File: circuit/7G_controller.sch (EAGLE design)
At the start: 19 parts, among them Q1 3.6864MHz

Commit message: 
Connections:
- new net AREF: ATMEGA169PV.AREF
- net N$5: no longer C5.+
- net N$6: now also C5.+
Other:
- moved on the sheet: C5
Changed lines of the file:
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@@
 <part name="P+5" library="SparkFun" deviceset="VCC" device=""/>
 <part name="GND4" library="SparkFun" deviceset="GND" device=""/>
+<part name="GND8" library="SparkFun" deviceset="GND" device=""/>
 </parts>
 <sheets>
@@
 <instance part="P+10" gate="1" x="63.5" y="-20.32"/>
 <instance part="GND7" gate="1" x="63.5" y="-35.56"/>
-<instance part="C5" gate="G$1" x="157.48" y="35.56"/>
+<instance part="C5" gate="G$1" x="142.24" y="58.42" rot="R270"/>
 <instance part="R2" gate="G$1" x="132.08" y="-7.62"/>
 <instance part="R3" gate="G$1" x="114.3" y="-2.54"/>
@@
 <instance part="P+5" gate="1" x="-43.18" y="12.7"/>
 <instance part="GND4" gate="1" x="-45.72" y="25.4" rot="R90"/>
+<instance part="GND8" gate="1" x="129.54" y="50.8"/>
 </instances>
 <busses>
@@
 </segment>
 <segment>
+<pinref part="GND6" gate="1" pin="GND"/>
 <pinref part="LP2980" gate="G$1" pin="GND"/>
-<pinref part="GND6" gate="1" pin="GND"/>
-<wire x1="170.18" y1="30.48" x2="170.18" y2="27.94" width="0.1524" layer="91"/>
-<pinref part="C5" gate="G$1" pin="-"/>
-<wire x1="170.18" y1="27.94" x2="170.18" y2="25.4" width="0.1524" layer="91"/>
-<wire x1="157.48" y1="30.48" x2="157.48" y2="27.94" width="0.1524" layer="91"/>
-<wire x1="157.48" y1="27.94" x2="170.18" y2="27.94" width="0.1524" layer="91"/>
-<junction x="170.18" y="27.94"/>
+<wire x1="170.18" y1="30.48" x2="170.18" y2="25.4" width="0.1524" layer="91"/>
 </segment>
 <segment>
@@
 <wire x1="-58.42" y1="15.24" x2="-58.42" y2="17.78" width="0.1524" layer="91"/>
 <junction x="-58.42" y="17.78"/>
+</segment>
+<segment>
+<pinref part="C5" gate="G$1" pin="-"/>
+<wire x1="137.16" y1="58.42" x2="129.54" y2="58.42" width="0.1524" layer="91"/>
+<wire x1="129.54" y1="58.42" x2="129.54" y2="53.34" width="0.1524" layer="91"/>
+<pinref part="GND8" gate="1" pin="GND"/>
 </segment>
 </net>
@@
 <pinref part="SJ1" gate="G$1" pin="2"/>
 <wire x1="149.86" y1="58.42" x2="149.86" y2="48.26" width="0.1524" layer="91"/>
+<pinref part="C5" gate="G$1" pin="+"/>
+<wire x1="144.78" y1="58.42" x2="149.86" y2="58.42" width="0.1524" layer="91"/>
+<junction x="149.86" y="58.42"/>
 </segment>
 </net>
@@
 <pinref part="SJ1" gate="G$1" pin="1"/>
 <pinref part="LP2980" gate="G$1" pin="VOUT"/>
-<wire x1="154.94" y1="43.18" x2="157.48" y2="43.18" width="0.1524" layer="91"/>
-<pinref part="C5" gate="G$1" pin="+"/>
-<wire x1="157.48" y1="43.18" x2="160.02" y2="43.18" width="0.1524" layer="91"/>
-<wire x1="157.48" y1="43.18" x2="157.48" y2="38.1" width="0.1524" layer="91"/>
-<junction x="157.48" y="43.18"/>
+<wire x1="154.94" y1="43.18" x2="160.02" y2="43.18" width="0.1524" layer="91"/>
 </segment>
 </net>
@@
 </segment>
 </net>
+<net name="AREF" class="0">
+<segment>
+<pinref part="ATMEGA169PV" gate="G$1" pin="AREF"/>
+<wire x1="-7.62" y1="83.82" x2="-15.24" y2="83.82" width="0.1524" layer="91"/>
+</segment>
+</net>

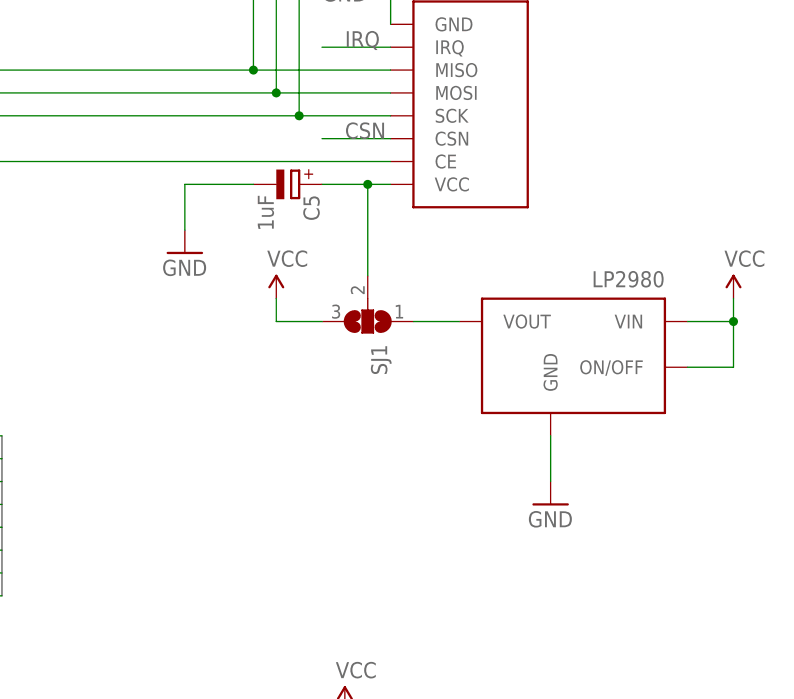
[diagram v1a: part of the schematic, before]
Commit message: 
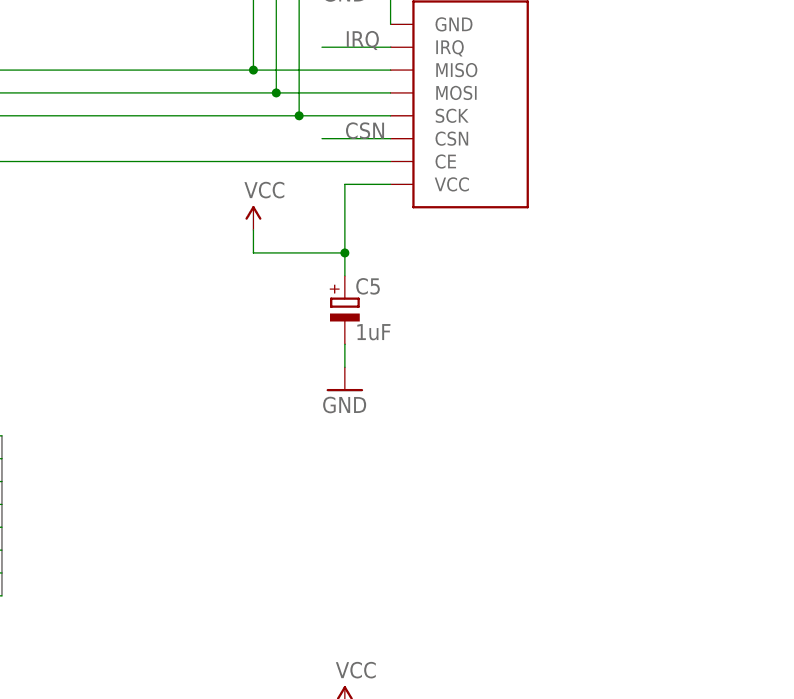
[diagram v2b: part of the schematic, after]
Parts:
- removed LP2980: LP2980, KileParts:LP2980
- removed SJ1: (no value), jumper:SJ2W
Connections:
- removed net N$5: LP2980.VOUT, SJ1.1
- removed net N$6: C5.+, NRF24L01.VCC, SJ1.2
- net GND: no longer LP2980.GND
- net VCC: now also C5.+, NRF24L01.VCC; no longer LP2980.ON/OFF, LP2980.VIN, SJ1.3
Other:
- moved on the sheet: C5
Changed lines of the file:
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@@
 <part name="P+7" library="SparkFun" deviceset="VCC" device=""/>
 <part name="P+8" library="SparkFun" deviceset="VCC" device=""/>
-<part name="LP2980" library="KileParts" deviceset="LP2980" device=""/>
-<part name="P+2" library="SparkFun" deviceset="VCC" device=""/>
-<part name="GND6" library="SparkFun" deviceset="GND" device=""/>
-<part name="SJ1" library="jumper" deviceset="SJ2W" device=""/>
-<part name="P+9" library="SparkFun" deviceset="VCC" device=""/>
 <part name="UART" library="KileParts" deviceset="UART_PORT" device=""/>
 <part name="P+10" library="SparkFun" deviceset="VCC" device=""/>
@@
 <part name="GND4" library="SparkFun" deviceset="GND" device=""/>
 <part name="GND8" library="SparkFun" deviceset="GND" device=""/>
+<part name="P+2" library="SparkFun" deviceset="VCC" device=""/>
 </parts>
 <sheets>
@@
 <instance part="P+7" gate="1" x="147.32" y="0"/>
 <instance part="P+8" gate="1" x="-15.24" y="-7.62"/>
-<instance part="LP2980" gate="G$1" x="172.72" y="38.1" rot="MR0"/>
-<instance part="P+2" gate="1" x="139.7" y="45.72"/>
-<instance part="GND6" gate="1" x="170.18" y="22.86"/>
-<instance part="SJ1" gate="G$1" x="149.86" y="43.18" rot="R270"/>
-<instance part="P+9" gate="1" x="190.5" y="45.72"/>
 <instance part="UART" gate="1" x="43.18" y="-25.4" rot="MR180"/>
 <instance part="P+10" gate="1" x="63.5" y="-20.32"/>
 <instance part="GND7" gate="1" x="63.5" y="-35.56"/>
-<instance part="C5" gate="G$1" x="142.24" y="58.42" rot="R270"/>
+<instance part="C5" gate="G$1" x="147.32" y="45.72"/>
 <instance part="R2" gate="G$1" x="132.08" y="-7.62"/>
 <instance part="R3" gate="G$1" x="114.3" y="-2.54"/>
@@
 <instance part="P+5" gate="1" x="-43.18" y="12.7"/>
 <instance part="GND4" gate="1" x="-45.72" y="25.4" rot="R90"/>
-<instance part="GND8" gate="1" x="129.54" y="50.8"/>
+<instance part="GND8" gate="1" x="147.32" y="35.56"/>
+<instance part="P+2" gate="1" x="137.16" y="53.34"/>
 </instances>
 <busses>
@@
 </segment>
 <segment>
-<pinref part="SJ1" gate="G$1" pin="3"/>
-<pinref part="P+2" gate="1" pin="VCC"/>
-<wire x1="144.78" y1="43.18" x2="139.7" y2="43.18" width="0.1524" layer="91"/>
-<wire x1="139.7" y1="43.18" x2="139.7" y2="45.72" width="0.1524" layer="91"/>
-</segment>
-<segment>
-<pinref part="LP2980" gate="G$1" pin="VIN"/>
-<pinref part="P+9" gate="1" pin="VCC"/>
-<wire x1="185.42" y1="43.18" x2="190.5" y2="43.18" width="0.1524" layer="91"/>
-<wire x1="190.5" y1="43.18" x2="190.5" y2="45.72" width="0.1524" layer="91"/>
-<pinref part="LP2980" gate="G$1" pin="ON/OFF"/>
-<wire x1="185.42" y1="38.1" x2="190.5" y2="38.1" width="0.1524" layer="91"/>
-<wire x1="190.5" y1="38.1" x2="190.5" y2="43.18" width="0.1524" layer="91"/>
-<junction x="190.5" y="43.18"/>
-</segment>
-<segment>
 <pinref part="UART" gate="1" pin="TX"/>
 <wire x1="50.8" y1="-25.4" x2="63.5" y2="-25.4" width="0.1524" layer="91"/>
@@
 <wire x1="-60.96" y1="10.16" x2="-43.18" y2="10.16" width="0.1524" layer="91"/>
 <wire x1="-43.18" y1="10.16" x2="-43.18" y2="12.7" width="0.1524" layer="91"/>
+</segment>
+<segment>
+<pinref part="NRF24L01" gate="G$1" pin="VCC"/>
+<pinref part="C5" gate="G$1" pin="+"/>
+<wire x1="147.32" y1="48.26" x2="147.32" y2="50.8" width="0.1524" layer="91"/>
+<wire x1="147.32" y1="50.8" x2="147.32" y2="58.42" width="0.1524" layer="91"/>
+<wire x1="147.32" y1="58.42" x2="152.4" y2="58.42" width="0.1524" layer="91"/>
+<pinref part="P+2" gate="1" pin="VCC"/>
+<wire x1="137.16" y1="53.34" x2="137.16" y2="50.8" width="0.1524" layer="91"/>
+<wire x1="137.16" y1="50.8" x2="147.32" y2="50.8" width="0.1524" layer="91"/>
+<junction x="147.32" y="50.8"/>
 </segment>
 </net>
@@
 </segment>
 <segment>
-<pinref part="GND6" gate="1" pin="GND"/>
-<pinref part="LP2980" gate="G$1" pin="GND"/>
-<wire x1="170.18" y1="30.48" x2="170.18" y2="25.4" width="0.1524" layer="91"/>
-</segment>
-<segment>
 <pinref part="UART" gate="1" pin="RX"/>
 <wire x1="50.8" y1="-27.94" x2="63.5" y2="-27.94" width="0.1524" layer="91"/>
@@
 <segment>
 <pinref part="C5" gate="G$1" pin="-"/>
-<wire x1="137.16" y1="58.42" x2="129.54" y2="58.42" width="0.1524" layer="91"/>
-<wire x1="129.54" y1="58.42" x2="129.54" y2="53.34" width="0.1524" layer="91"/>
 <pinref part="GND8" gate="1" pin="GND"/>
+<wire x1="147.32" y1="38.1" x2="147.32" y2="40.64" width="0.1524" layer="91"/>
 </segment>
 </net>
@@
 </segment>
 </net>
-<net name="N$6" class="0">
-<segment>
-<pinref part="NRF24L01" gate="G$1" pin="VCC"/>
-<wire x1="149.86" y1="58.42" x2="152.4" y2="58.42" width="0.1524" layer="91"/>
-<pinref part="SJ1" gate="G$1" pin="2"/>
-<wire x1="149.86" y1="58.42" x2="149.86" y2="48.26" width="0.1524" layer="91"/>
-<pinref part="C5" gate="G$1" pin="+"/>
-<wire x1="144.78" y1="58.42" x2="149.86" y2="58.42" width="0.1524" layer="91"/>
-<junction x="149.86" y="58.42"/>
-</segment>
-</net>
 <net name="LEDSCRL" class="0">
 <segment>
@@
 </segment>
 </net>
-<net name="N$5" class="0">
-<segment>
-<pinref part="SJ1" gate="G$1" pin="1"/>
-<pinref part="LP2980" gate="G$1" pin="VOUT"/>
-<wire x1="154.94" y1="43.18" x2="160.02" y2="43.18" width="0.1524" layer="91"/>
-</segment>
-</net>

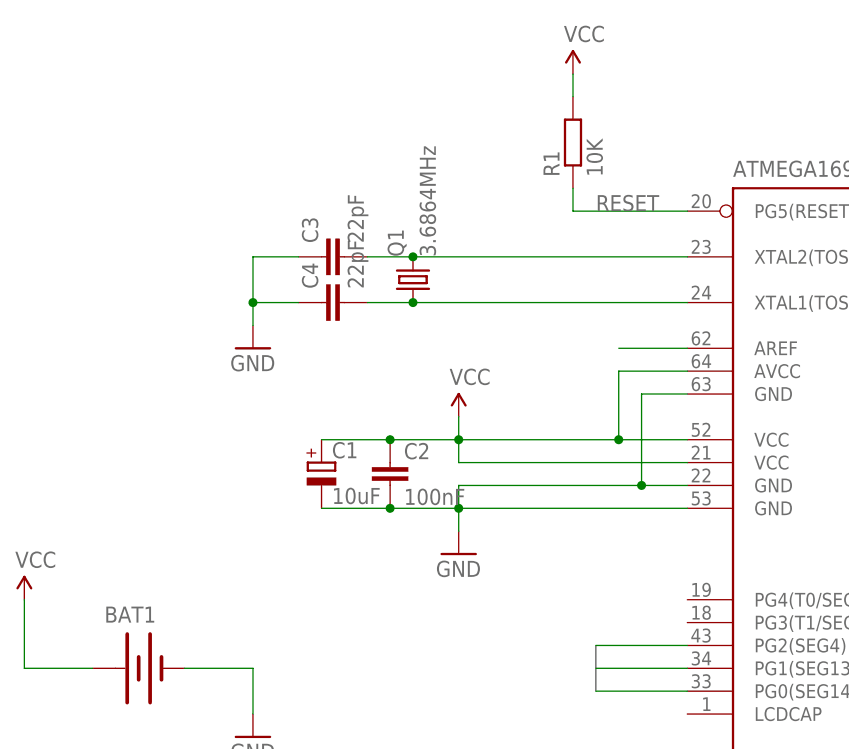
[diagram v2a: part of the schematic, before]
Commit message: 
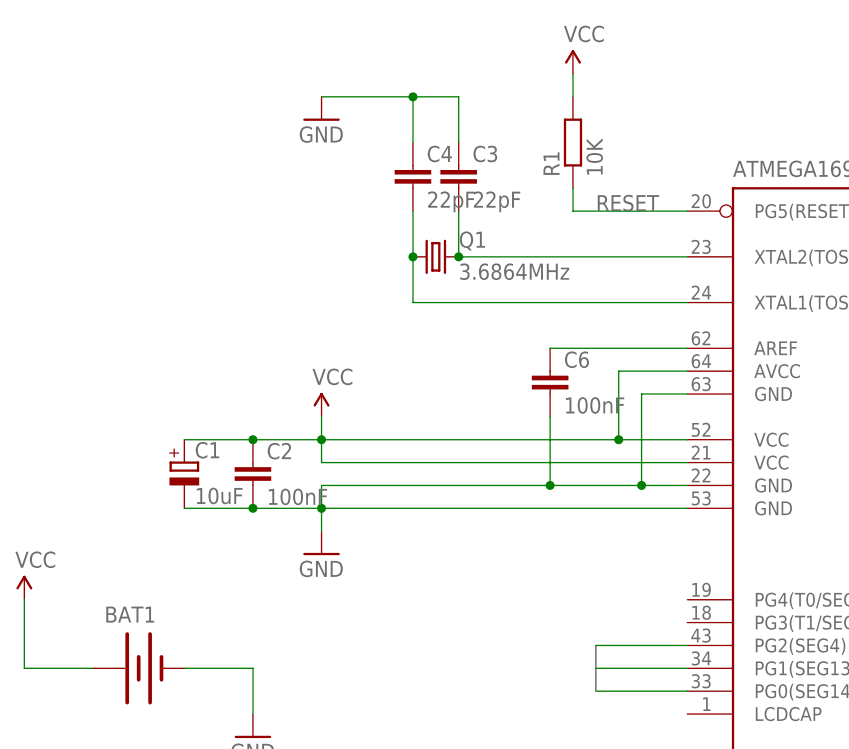
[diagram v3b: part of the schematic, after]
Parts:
- added C6: 100nF, rcl:C-EUC0805
- Q1: device SparkFun:CRYSTALHC49UV -> crystal:CRYSTALTC26H
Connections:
- net AREF: now also C6.1
- net GND: now also C6.2
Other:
- moved on the sheet: C1, C2, C3, C4, Q1

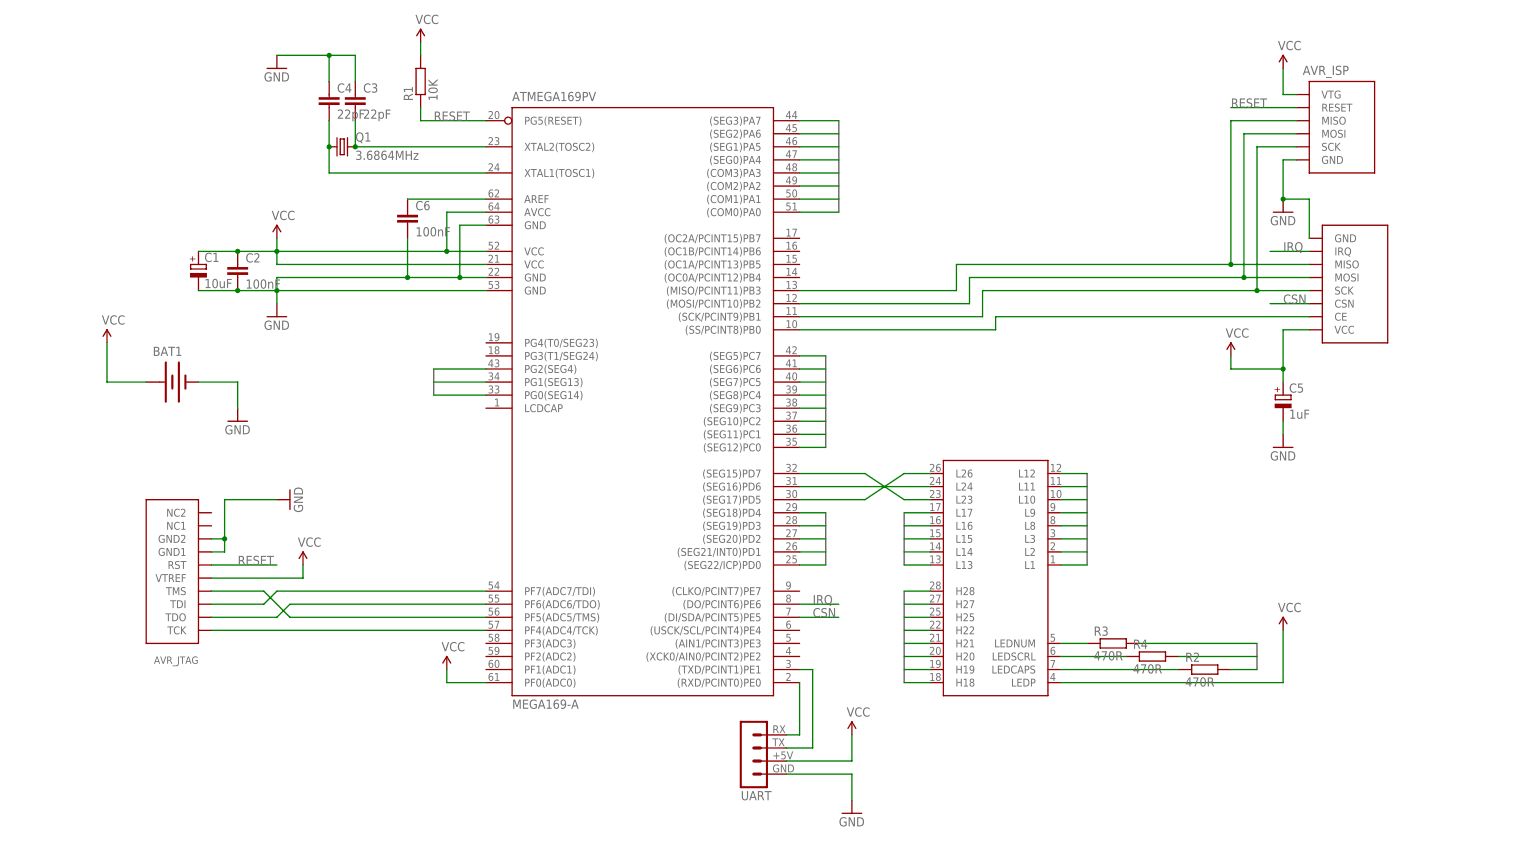
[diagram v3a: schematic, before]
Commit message: 
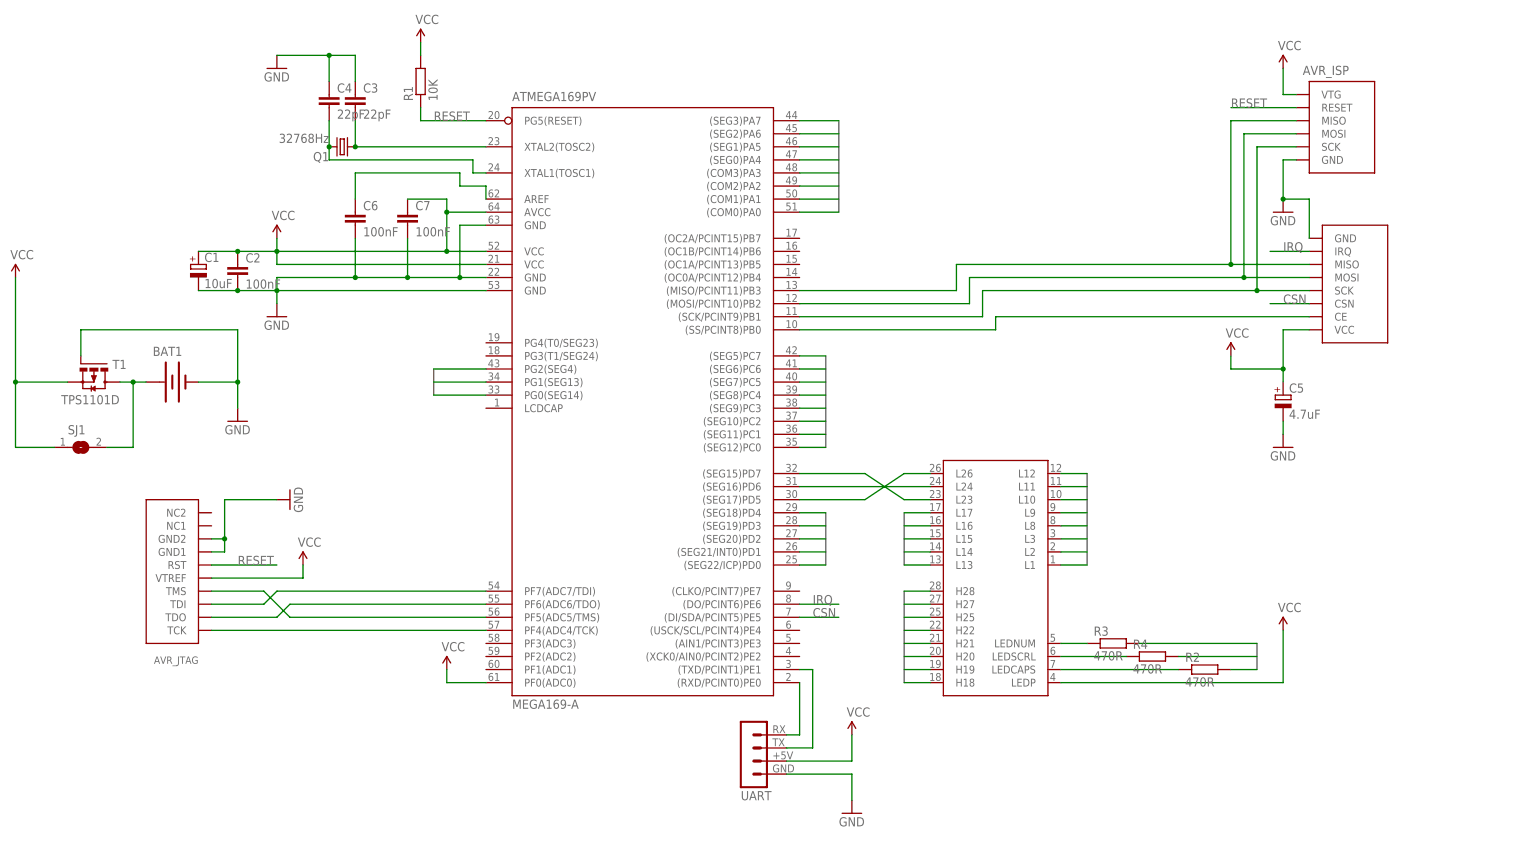
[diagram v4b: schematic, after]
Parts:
- added C7: 100nF, rcl:C-EUC0805
- added SJ1: (no value), jumper:SJ
- added T1: TPS1101D, KileParts:TPS1101D
- C5: value 1uF -> 4.7uF
- NRF24L01: value NRF24L01_MOD_NINE_EAGLES -> NRF24L01_MOD_NINE_EAGLESGENERIC; device KileParts:NRF24L01_MOD_NINE_EAGLES -> KileParts:NRF24L01_MOD_NINE_EAGLESGENERIC
- Q1: value 3.6864MHz -> 32768Hz; device crystal:CRYSTALTC26H -> KileParts:CRYSTAL
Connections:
- removed net N$7: ATMEGA169PV.XTAL2(TOSC2), C3.2, Q1.2
- new net N$4: BAT1.+, SJ1.2, T1.D
- new net N$6: ATMEGA169PV.XTAL2(TOSC2), C3.2, Q1.1
- net GND: now also C7.2, T1.G
- net N$8: now also Q1.2; no longer Q1.1
- net VCC: now also C7.1, SJ1.1, T1.S; no longer BAT1.+
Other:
- moved on the sheet: C6, Q1

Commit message: renamed avr_serial -> avrdbg
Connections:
- net VCC: no longer ATMEGA169PV.PF0(ADC0)
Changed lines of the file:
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@@
 <part name="GND5" library="SparkFun" deviceset="GND" device=""/>
 <part name="P+7" library="SparkFun" deviceset="VCC" device=""/>
-<part name="P+8" library="SparkFun" deviceset="VCC" device=""/>
 <part name="UART" library="KileParts" deviceset="UART_PORT" device=""/>
 <part name="P+10" library="SparkFun" deviceset="VCC" device=""/>
@@
 <instance part="GND5" gate="1" x="-55.88" y="40.64"/>
 <instance part="P+7" gate="1" x="147.32" y="0"/>
-<instance part="P+8" gate="1" x="-15.24" y="-7.62"/>
 <instance part="UART" gate="1" x="43.18" y="-25.4" rot="MR180"/>
 <instance part="P+10" gate="1" x="63.5" y="-20.32"/>
@@
 <wire x1="147.32" y1="-10.16" x2="147.32" y2="0" width="0.1524" layer="91"/>
 <pinref part="P+7" gate="1" pin="VCC"/>
-</segment>
-<segment>
-<pinref part="ATMEGA169PV" gate="G$1" pin="PF0(ADC0)"/>
-<pinref part="P+8" gate="1" pin="VCC"/>
-<wire x1="-7.62" y1="-10.16" x2="-15.24" y2="-10.16" width="0.1524" layer="91"/>
-<wire x1="-15.24" y1="-10.16" x2="-15.24" y2="-7.62" width="0.1524" layer="91"/>
 </segment>
 <segment>
@@
 <segment>
 <pinref part="ATMEGA169PV" gate="G$1" pin="XTAL1(TOSC1)"/>
-<wire x1="-7.62" y1="88.9" x2="-10.16" y2="88.9" width="0.1524" layer="91"/>
-<wire x1="-10.16" y1="88.9" x2="-10.16" y2="91.44" width="0.1524" layer="91"/>
-<wire x1="-10.16" y1="91.44" x2="-38.1" y2="91.44" width="0.1524" layer="91"/>
+<wire x1="-7.62" y1="88.9" x2="-38.1" y2="88.9" width="0.1524" layer="91"/>
 <pinref part="C4" gate="G$1" pin="2"/>
 <pinref part="Q1" gate="G$1" pin="2"/>
 <wire x1="-38.1" y1="99.06" x2="-38.1" y2="93.98" width="0.1524" layer="91"/>
-<wire x1="-38.1" y1="91.44" x2="-38.1" y2="93.98" width="0.1524" layer="91"/>
+<wire x1="-38.1" y1="88.9" x2="-38.1" y2="93.98" width="0.1524" layer="91"/>
 <junction x="-38.1" y="93.98"/>
 </segment>
@@
 <pinref part="ATMEGA169PV" gate="G$1" pin="AREF"/>
 <pinref part="C6" gate="G$1" pin="1"/>
-<wire x1="-7.62" y1="83.82" x2="-7.62" y2="86.36" width="0.1524" layer="91"/>
-<wire x1="-7.62" y1="86.36" x2="-12.7" y2="86.36" width="0.1524" layer="91"/>
-<wire x1="-12.7" y1="86.36" x2="-12.7" y2="88.9" width="0.1524" layer="91"/>
-<wire x1="-12.7" y1="88.9" x2="-33.02" y2="88.9" width="0.1524" layer="91"/>
-<wire x1="-33.02" y1="88.9" x2="-33.02" y2="83.82" width="0.1524" layer="91"/>
-</segment>
-</net>
+<wire x1="-7.62" y1="83.82" x2="-12.7" y2="83.82" width="0.1524" layer="91"/>
+<wire x1="-12.7" y1="83.82" x2="-12.7" y2="86.36" width="0.1524" layer="91"/>
+<wire x1="-12.7" y1="86.36" x2="-33.02" y2="86.36" width="0.1524" layer="91"/>
+<wire x1="-33.02" y1="86.36" x2="-33.02" y2="83.82" width="0.1524" layer="91"/>
+</segment>
+</net>
